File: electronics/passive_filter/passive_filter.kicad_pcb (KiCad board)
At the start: 2 copper layers, 2 parts

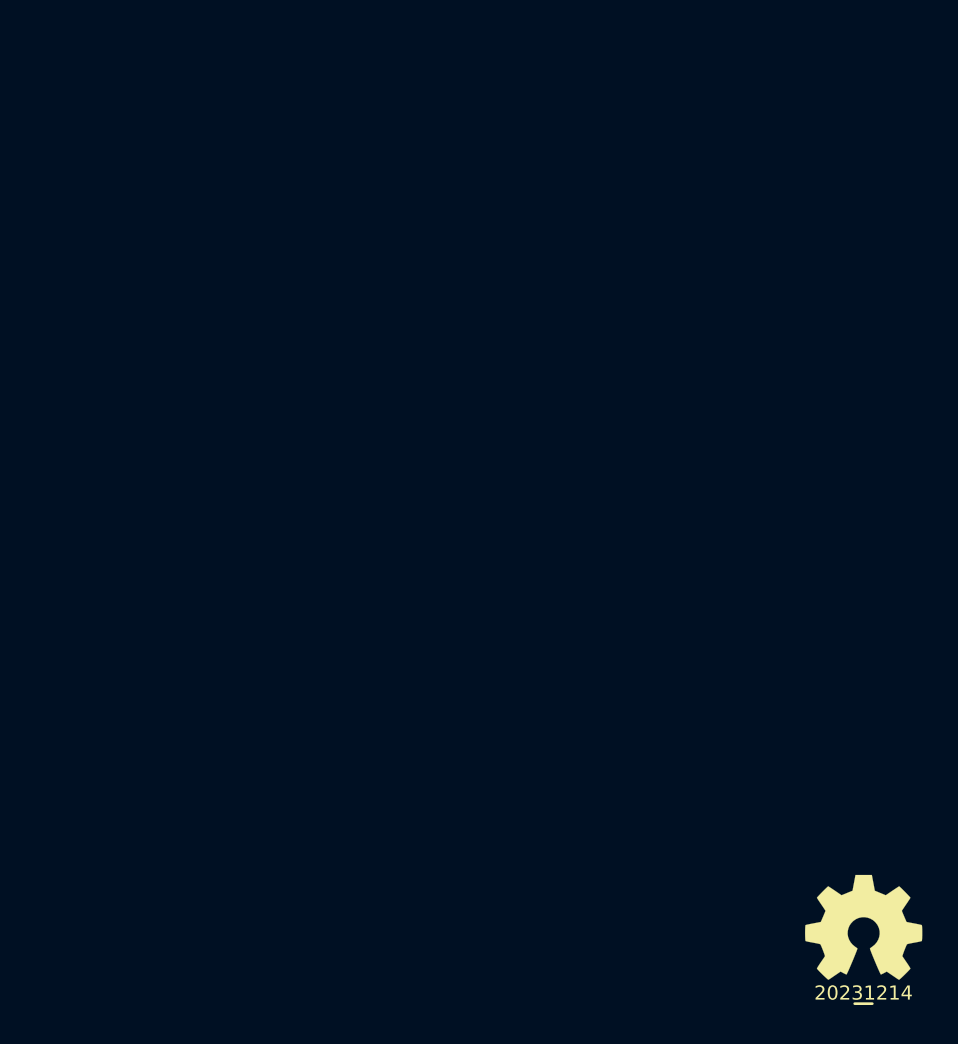
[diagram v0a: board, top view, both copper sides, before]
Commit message: completed passive filter
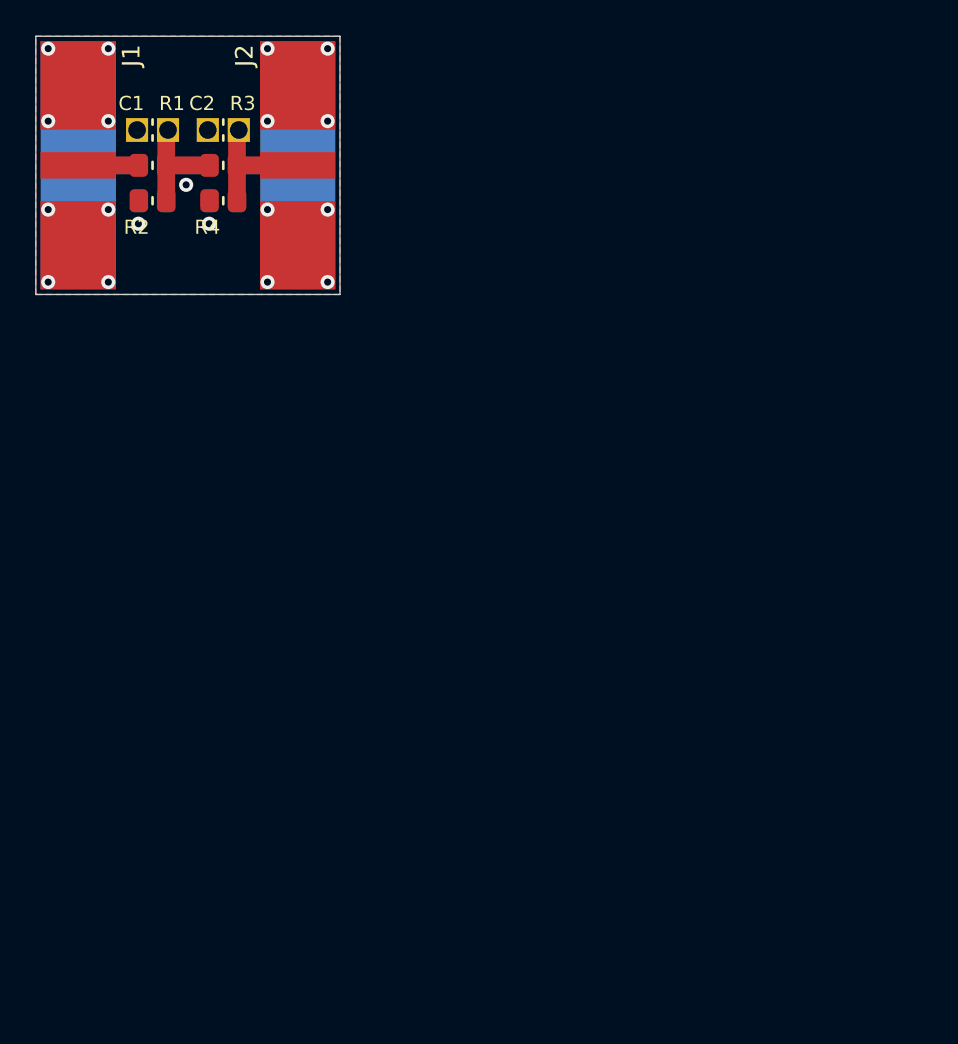
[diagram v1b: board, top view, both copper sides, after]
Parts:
- added C1: C, SquantorCapacitor:C_0402+0603+0805+TH, F.Cu at (98.5, 42.5)
- added C2: C, SquantorCapacitor:C_0402+0603+0805+TH, F.Cu at (102.5, 42.5)
- added J1: Coax, SquantorConnectors:coax_edge_1.5_center_5_side, F.Cu at (94.3, 44.5)
- added J2: Coax, SquantorConnectors:coax_edge_1.5_center_5_side, F.Cu at (106.7, 44.5)
- added R1: R, SquantorResistor:R_0805+0603, F.Cu at (98.5, 44.5)
- added R2: R, SquantorResistor:R_0805+0603, F.Cu at (98.5, 46.5)
- added R3: R, SquantorResistor:R_0805+0603, F.Cu at (102.5, 44.5)
- added R4: R, SquantorResistor:R_0805+0603, F.Cu at (102.5, 46.5)
- N1, N2: moved to B.Cu
- moved N1 55.7 mm to (100.5, 50.7), turned to 180 degrees
- moved N2 55.7 mm to (100.5, 47.0), turned to 180 degrees
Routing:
- net Net-(C2-Pad2): track 0.00 -> 7.47 mm
- net Net-(C1-Pad2): track 0.00 -> 6.49 mm
- net Net-(J1-Pad1): track 0.00 -> 3.44 mm
- net GND: vias 0 -> 19
- added copper zone on B.Cu, net GND
- added copper zone on F.Cu, net GND
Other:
- board outline added: 17.2 x 14.6 mm
